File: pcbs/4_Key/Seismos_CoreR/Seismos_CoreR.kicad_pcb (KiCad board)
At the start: 2 copper layers, 147 x 78 mm, 26 parts, among them J1 SM09B-SRSS-TB(LF)(SN), J2 SM09B-SRSS-TB(LF)(SN), J3 SM09B-SRSS-TB(LF)(SN), J4 SM09B-SRSS-TB(LF)(SN), J5 SM09B-SRSS-TB(LF)(SN), J6 SM09B-SRSS-TB(LF)(SN), J7 Conn_01x05_Pin, J8 MJ-4PP-9-Lily58, J9 SM09B-SRSS-TB(LF)(SN), SW1 RotaryEncoder_Switch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

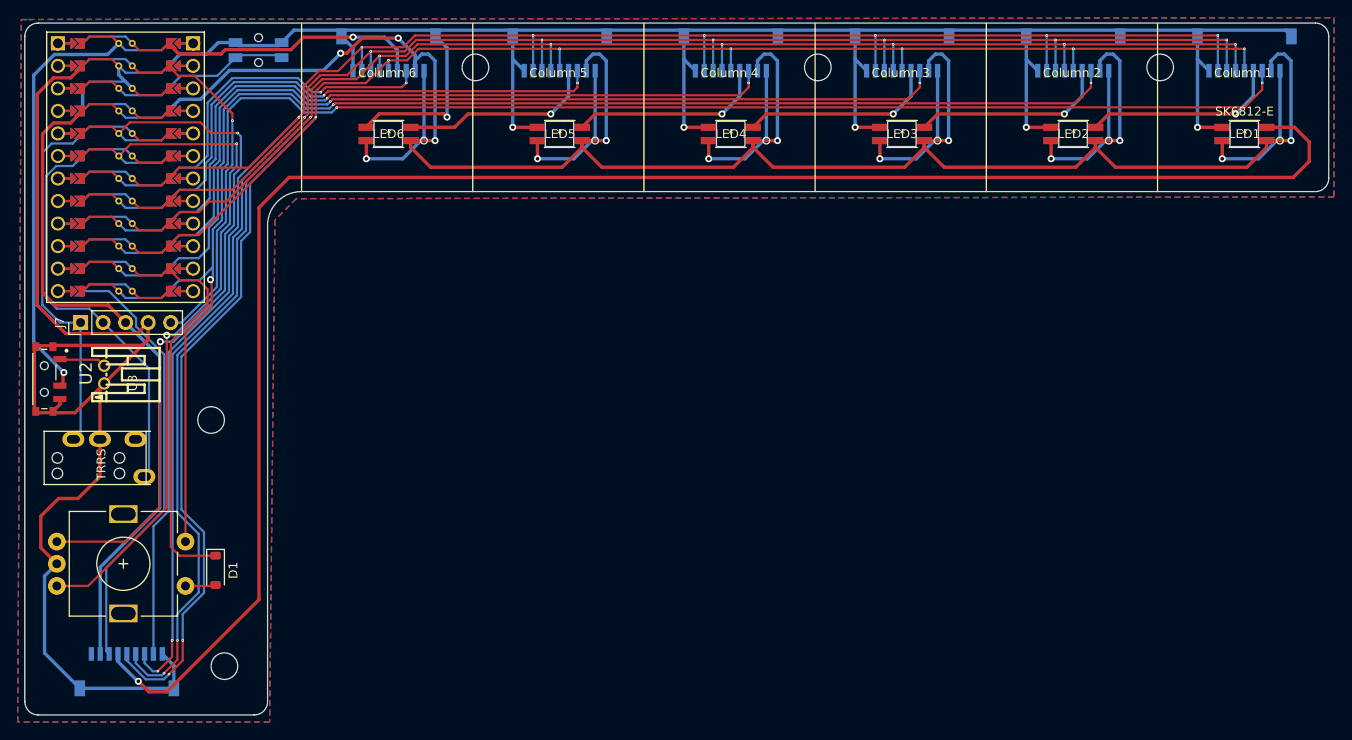
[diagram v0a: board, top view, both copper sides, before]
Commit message: Fix footprint errors and new 2x2 PCB
Fixed keyboard_reversible.pretty not being included.
Added a 2x2 PCB for the thumb.

Added a note regarding DRC errors involving two specific footprints...
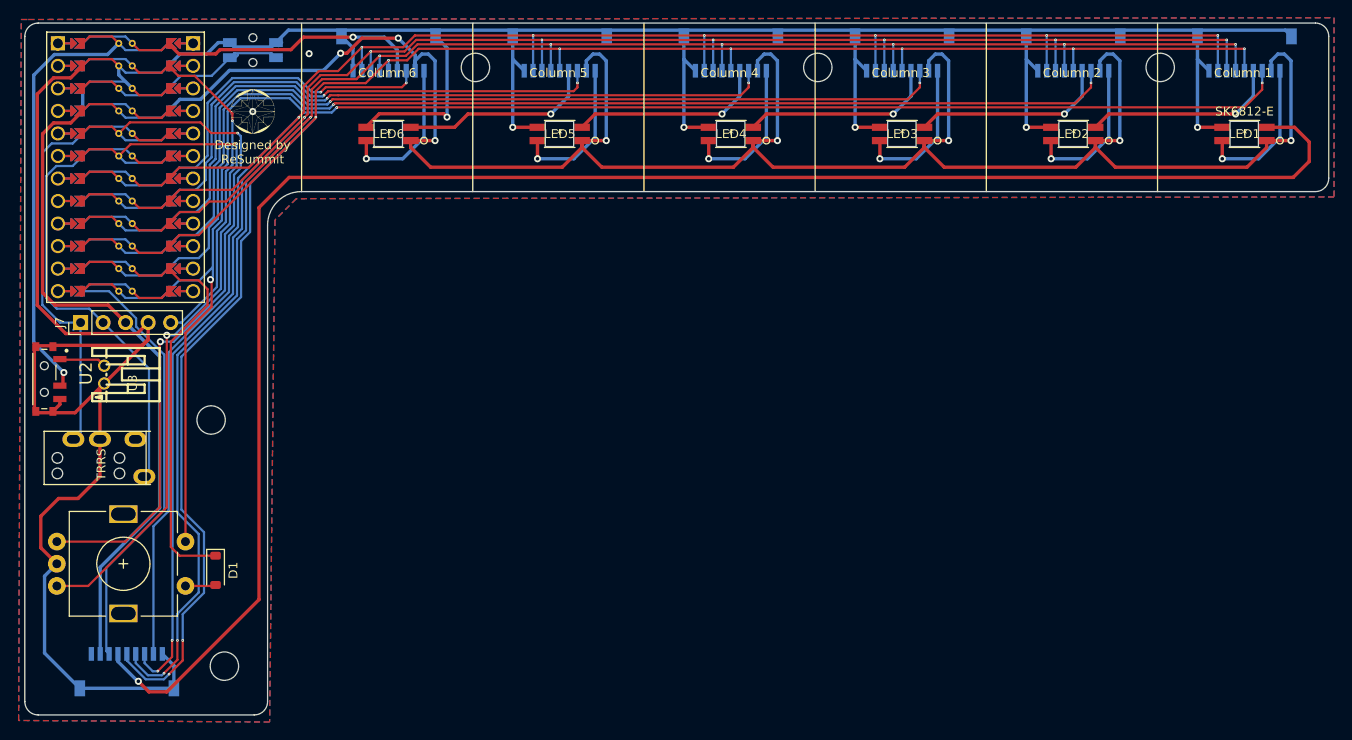
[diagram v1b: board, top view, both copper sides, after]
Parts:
- added G***: LOGO, Seismos-libs:ReSummit_Logo, F.Cu at (55.7, 30.0)
- ? (x5): value (none) -> Hole_M3_3.2mm; footprint (none) -> Seismos-libs:Hole_M3_3.2mm
- moved SW3 0.64 mm to (55.7, 23.0)
- turned ? to 180 degrees
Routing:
- net GND: track 374.6 -> 375.3 mm, vias 6 -> 8
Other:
- board text added: "Designed by ReSummit"
